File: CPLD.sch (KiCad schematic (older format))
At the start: 35 parts, among them J5 JTAG, SW2 SW_DIP_x06, SW3 User PB, U12 74HCT3G04, U3 EPM7064STC100, X1 CFPS-72 50mhz

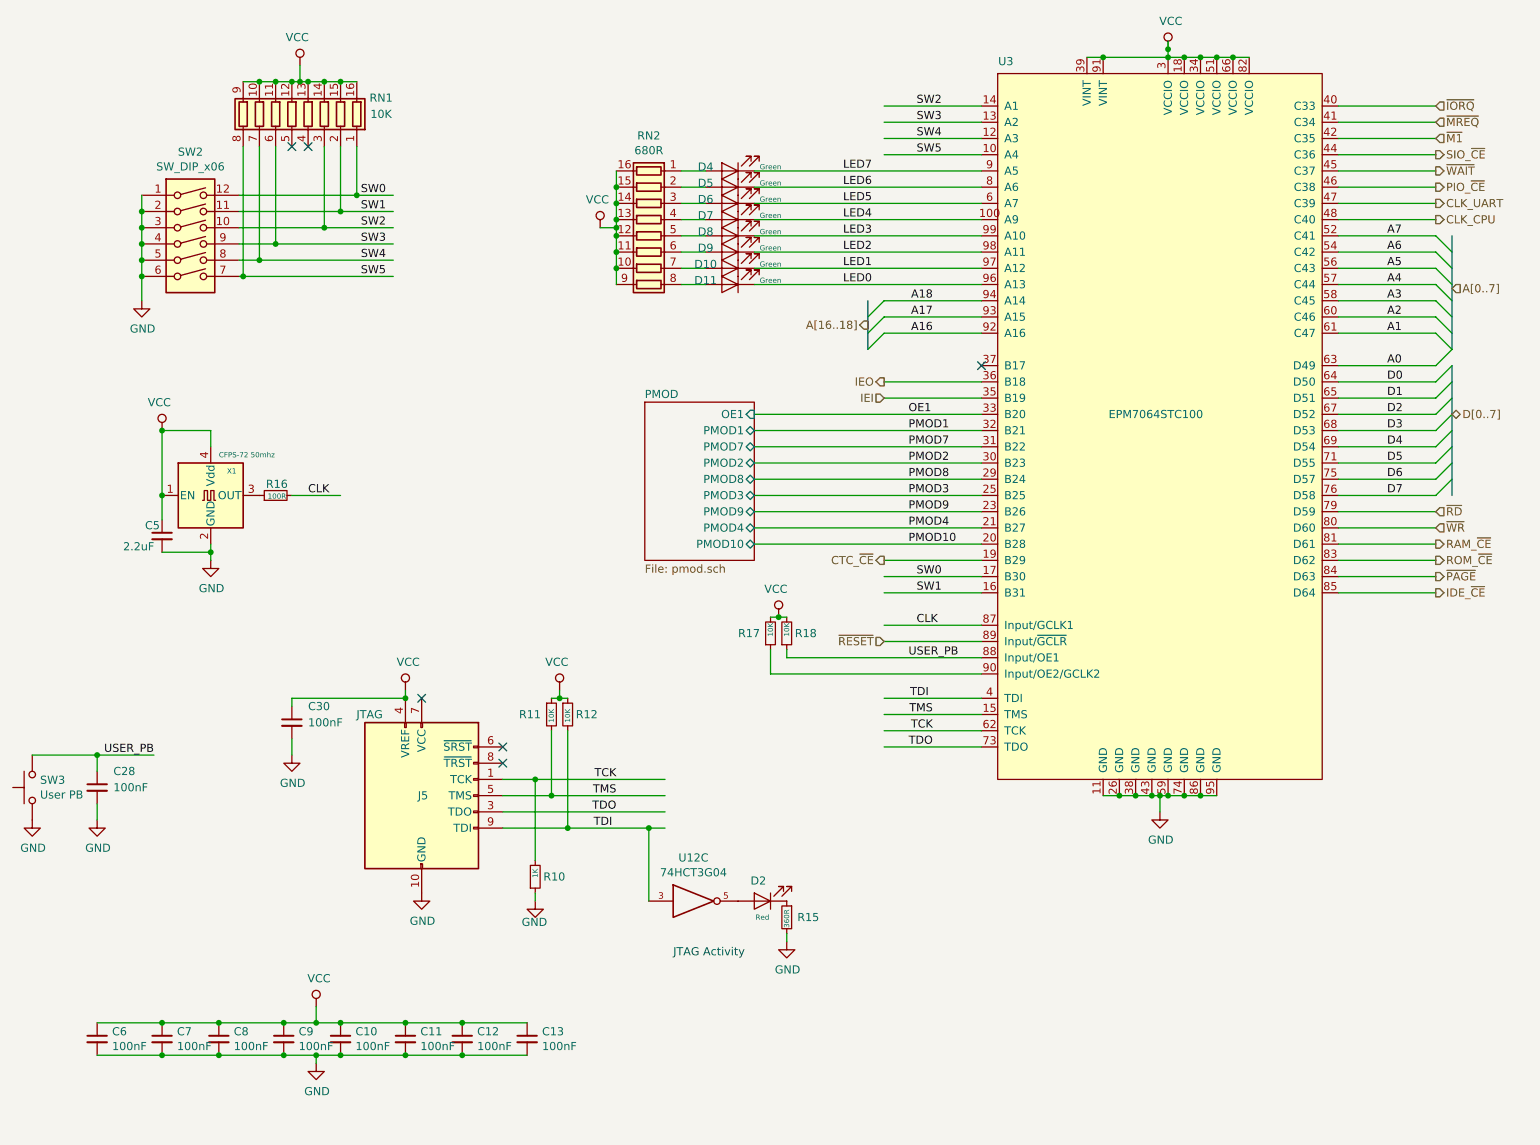
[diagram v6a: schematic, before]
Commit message: replaced VCC with 5V, fixed ROM footprint
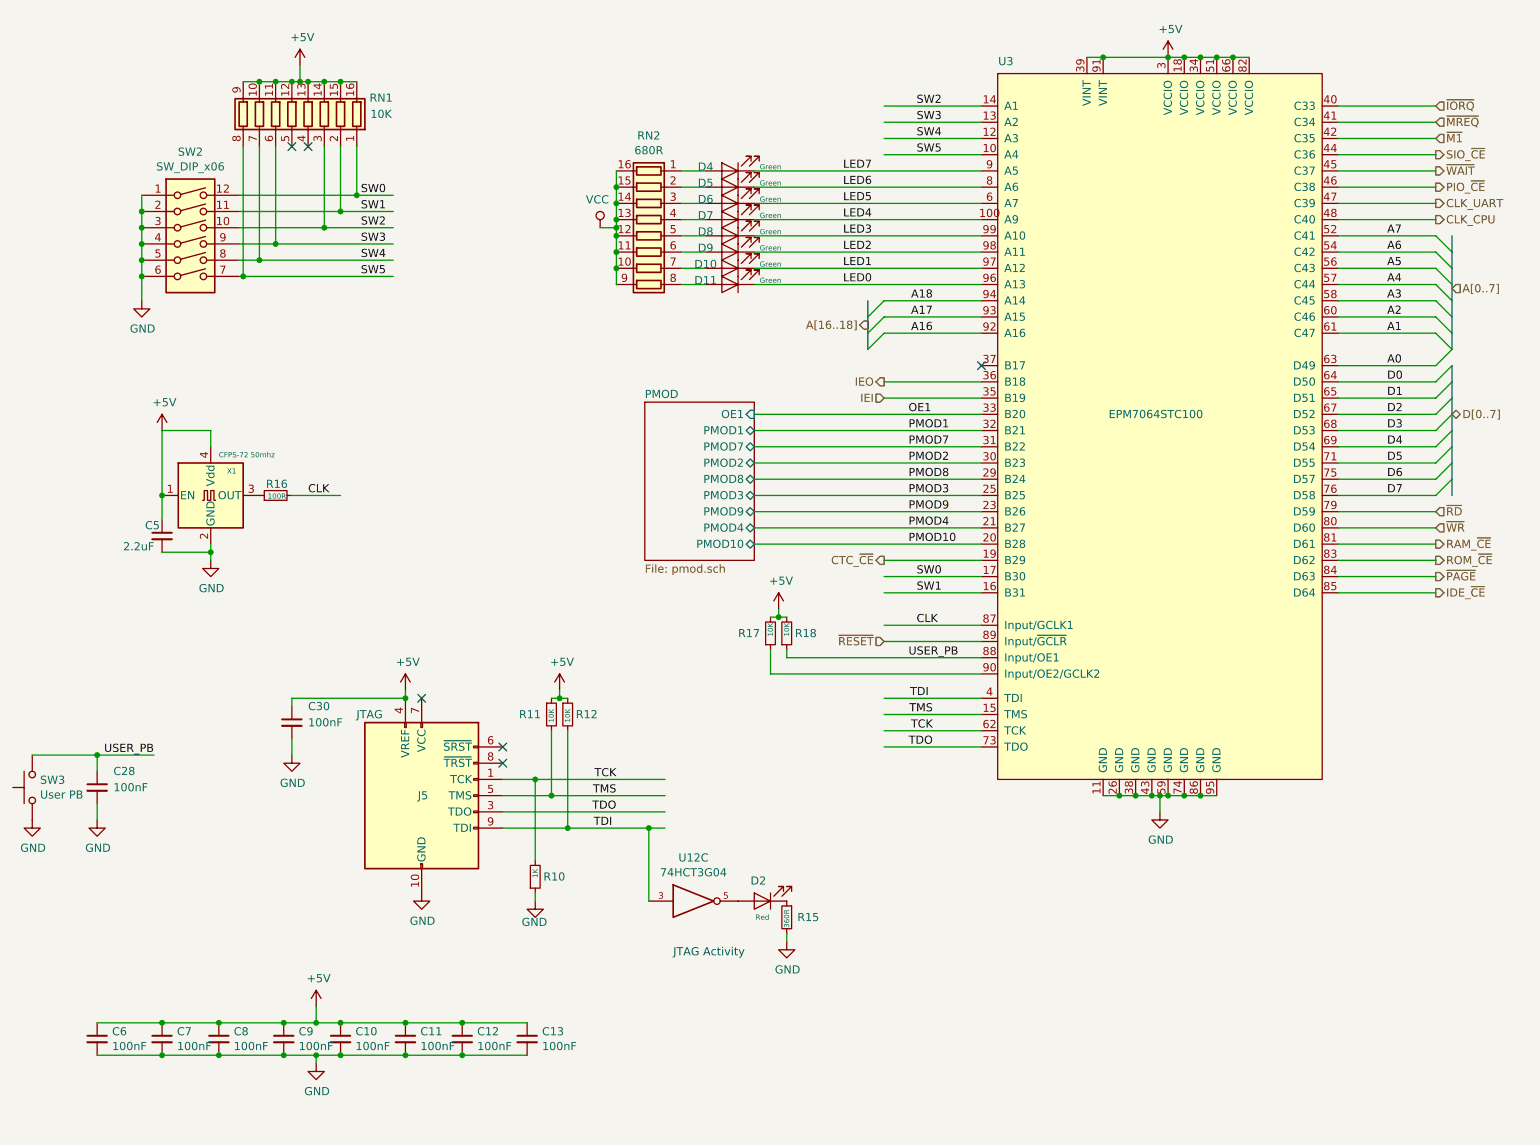
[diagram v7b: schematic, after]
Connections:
- net labels added: +5V
- wire segments 190 -> 189
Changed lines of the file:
@@
 	1    0    0    -1
-$EndComp
-Connection ~ 1700 3250
-$Comp
-L power:VCC #PWR?
-U 1 1 5DB43EF8
-P 1700 3250
-AR Path="/5DB43EF8" Ref="#PWR?"  Part="1"
-AR Path="/5D70CA34/5DB43EF8" Ref="#PWR023"  Part="1"
-F 0 "#PWR023" H 1700 3100 50  0001 C CNN
-F 1 "VCC" H 1717 3423 50  0000 C CNN
-F 2 "" H 1700 3250 50  0001 C CNN
-F 3 "" H 1700 3250 50  0001 C CNN
-	1    1700 3250
-	-1   0    0    -1
 $EndComp
 $Comp
@@
 	-1   0    0    -1
 $EndComp
-$Comp
-L power:VCC #PWR?
-U 1 1 5DC12FAB
-P 3200 4850
-AR Path="/5DC12FAB" Ref="#PWR?"  Part="1"
-AR Path="/5D70CA34/5DC12FAB" Ref="#PWR020"  Part="1"
-F 0 "#PWR020" H 3200 4700 50  0001 C CNN
-F 1 "VCC" H 3217 5023 50  0000 C CNN
-F 2 "" H 3200 4850 50  0001 C CNN
-F 3 "" H 3200 4850 50  0001 C CNN
-	1    3200 4850
-	1    0    0    -1
-$EndComp
 Wire Wire Line
 	3800 5400 4000 5400
@@
 $EndComp
 Connection ~ 7900 950
-$Comp
-L power:VCC #PWR?
-U 1 1 5DF027A6
-P 7900 900
-AR Path="/5DF027A6" Ref="#PWR?"  Part="1"
-AR Path="/5D70CA34/5DF027A6" Ref="#PWR032"  Part="1"
-F 0 "#PWR032" H 7900 750 50  0001 C CNN
-F 1 "VCC" H 7917 1073 50  0000 C CNN
-F 2 "" H 7900 900 50  0001 C CNN
-F 3 "" H 7900 900 50  0001 C CNN
-	1    7900 900
-	1    0    0    -1
-$EndComp
-Wire Wire Line
-	7900 950  7900 900
 Wire Wire Line
 	7850 5500 7850 5600
@@
 Wire Wire Line
 	3550 7100 3200 7100
-$Comp
-L power:VCC #PWR?
-U 1 1 5FB8A6EC
-P 2650 6800
-AR Path="/5FB8A6EC" Ref="#PWR?"  Part="1"
-AR Path="/5D70CA34/5FB8A6EC" Ref="#PWR029"  Part="1"
-F 0 "#PWR029" H 2650 6650 50  0001 C CNN
-F 1 "VCC" H 2667 6973 50  0000 C CNN
-F 2 "" H 2650 6800 50  0001 C CNN
-F 3 "" H 2650 6800 50  0001 C CNN
-	1    2650 6800
-	1    0    0    -1
-$EndComp
 Wire Wire Line
 	2650 6900 2650 6800
@@
 OE1
 NoConn ~ 6750 2850
-Connection ~ 7900 900
-Wire Wire Line
-	7900 900  7900 850
 Wire Wire Line
 	5350 1750 6750 1750
@@
 Wire Wire Line
 	5350 1650 6750 1650
-$Comp
-L power:VCC #PWR?
-U 1 1 5D9F3379
-P 5500 4400
-AR Path="/5D9F3379" Ref="#PWR?"  Part="1"
-AR Path="/5D70CA34/5D9F3379" Ref="#PWR0102"  Part="1"
-F 0 "#PWR0102" H 5500 4250 50  0001 C CNN
-F 1 "VCC" H 5517 4573 50  0000 C CNN
-F 2 "" H 5500 4400 50  0001 C CNN
-F 3 "" H 5500 4400 50  0001 C CNN
-	1    5500 4400
-	-1   0    0    -1
-$EndComp
 Text Label 2600 3650 0    50   ~ 0
 CLK
@@
 Wire Wire Line
 	2550 1100 2500 1100
-$Comp
-L power:VCC #PWR024
-U 1 1 5D7E678A
-P 2550 1000
-F 0 "#PWR024" H 2550 850 50  0001 C CNN
-F 1 "VCC" H 2567 1173 50  0000 C CNN
-F 2 "" H 2550 1000 50  0001 C CNN
-F 3 "" H 2550 1000 50  0001 C CNN
-	1    2550 1000
-	-1   0    0    -1
-$EndComp
 Wire Wire Line
 	2700 1500 2700 2000
@@
 IEO
 Wire Wire Line
-	5450 4400 5500 4400
-Connection ~ 5500 4400
-Wire Wire Line
-	5500 4400 5550 4400
-Wire Wire Line
 	5550 4600 5550 4650
 Wire Wire Line
@@
 Wire Wire Line
 	3800 5700 4200 5700
-$Comp
-L power:VCC #PWR?
-U 1 1 5DA39994
-P 4150 4850
-AR Path="/5DA39994" Ref="#PWR?"  Part="1"
-AR Path="/5D70CA34/5DA39994" Ref="#PWR022"  Part="1"
-F 0 "#PWR022" H 4150 4700 50  0001 C CNN
-F 1 "VCC" H 4167 5023 50  0000 C CNN
-F 2 "" H 4150 4850 50  0001 C CNN
-F 3 "" H 4150 4850 50  0001 C CNN
-	1    4150 4850
-	-1   0    0    -1
-$EndComp
 Wire Wire Line
 	4150 4850 4150 4900
@@
 	2500 4900 3200 4900
 Connection ~ 3200 4900
+$Comp
+L power:+5V #PWR?
+U 1 1 5EB28D79
+P 7900 950
+AR Path="/5D70CA34/5DC790D1/5EB28D79" Ref="#PWR?"  Part="1"
+AR Path="/5D70CA34/5EB28D79" Ref="#PWR0121"  Part="1"
+F 0 "#PWR0121" H 7900 800 50  0001 C CNN
+F 1 "+5V" H 7915 1123 50  0000 C CNN
+F 2 "" H 7900 950 50  0001 C CNN
+F 3 "" H 7900 950 50  0001 C CNN
+	1    7900 950
+	1    0    0    -1
+$EndComp
+$Comp
+L power:+5V #PWR?
+U 1 1 5EB440A1
+P 2550 1000
+AR Path="/5D70CA34/5DC790D1/5EB440A1" Ref="#PWR?"  Part="1"
+AR Path="/5D70CA34/5EB440A1" Ref="#PWR0122"  Part="1"
+F 0 "#PWR0122" H 2550 850 50  0001 C CNN
+F 1 "+5V" H 2565 1173 50  0000 C CNN
+F 2 "" H 2550 1000 50  0001 C CNN
+F 3 "" H 2550 1000 50  0001 C CNN
+	1    2550 1000
+	1    0    0    -1
+$EndComp
+$Comp
+L power:+5V #PWR?
+U 1 1 5EB7B4D6
+P 1700 3250
+AR Path="/5D70CA34/5DC790D1/5EB7B4D6" Ref="#PWR?"  Part="1"
+AR Path="/5D70CA34/5EB7B4D6" Ref="#PWR0123"  Part="1"
+F 0 "#PWR0123" H 1700 3100 50  0001 C CNN
+F 1 "+5V" H 1715 3423 50  0000 C CNN
+F 2 "" H 1700 3250 50  0001 C CNN
+F 3 "" H 1700 3250 50  0001 C CNN
+	1    1700 3250
+	1    0    0    -1
+$EndComp
+$Comp
+L power:+5V #PWR?
+U 1 1 5EB9676C
+P 3200 4850
+AR Path="/5D70CA34/5DC790D1/5EB9676C" Ref="#PWR?"  Part="1"
+AR Path="/5D70CA34/5EB9676C" Ref="#PWR0124"  Part="1"
+F 0 "#PWR0124" H 3200 4700 50  0001 C CNN
+F 1 "+5V" H 3215 5023 50  0000 C CNN
+F 2 "" H 3200 4850 50  0001 C CNN
+F 3 "" H 3200 4850 50  0001 C CNN
+	1    3200 4850
+	1    0    0    -1
+$EndComp
+$Comp
+L power:+5V #PWR?
+U 1 1 5EBB1BE7
+P 4150 4850
+AR Path="/5D70CA34/5DC790D1/5EBB1BE7" Ref="#PWR?"  Part="1"
+AR Path="/5D70CA34/5EBB1BE7" Ref="#PWR0125"  Part="1"
+F 0 "#PWR0125" H 4150 4700 50  0001 C CNN
+F 1 "+5V" H 4165 5023 50  0000 C CNN
+F 2 "" H 4150 4850 50  0001 C CNN
+F 3 "" H 4150 4850 50  0001 C CNN
+	1    4150 4850
+	1    0    0    -1
+$EndComp
+$Comp
+L power:+5V #PWR?
+U 1 1 5EBCCE40
+P 2650 6800
+AR Path="/5D70CA34/5DC790D1/5EBCCE40" Ref="#PWR?"  Part="1"
+AR Path="/5D70CA34/5EBCCE40" Ref="#PWR0126"  Part="1"
+F 0 "#PWR0126" H 2650 6650 50  0001 C CNN
+F 1 "+5V" H 2665 6973 50  0000 C CNN
+F 2 "" H 2650 6800 50  0001 C CNN
+F 3 "" H 2650 6800 50  0001 C CNN
+	1    2650 6800
+	1    0    0    -1
+$EndComp
+Wire Wire Line
+	5450 4400 5500 4400
+$Comp
+L power:+5V #PWR?
+U 1 1 5F1064BC
+P 5500 4350
+AR Path="/5D70CA34/5DC790D1/5F1064BC" Ref="#PWR?"  Part="1"
+AR Path="/5D70CA34/5F1064BC" Ref="#PWR0127"  Part="1"
+F 0 "#PWR0127" H 5500 4200 50  0001 C CNN
+F 1 "+5V" H 5515 4523 50  0000 C CNN
+F 2 "" H 5500 4350 50  0001 C CNN
+F 3 "" H 5500 4350 50  0001 C CNN
+	1    5500 4350
+	1    0    0    -1
+$EndComp
+Wire Wire Line
+	5500 4350 5500 4400
 Wire Bus Line
 	6050 2450 6050 2750
@@
 Wire Bus Line
 	9650 2850 9650 3650
+Connection ~ 5500 4400
+Wire Wire Line
+	5500 4400 5550 4400
 $EndSCHEMATC

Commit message: layout changes, silkscreen fixes
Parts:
- U8: renamed from U12; value 74HCT3G04 -> 74LVC1G04; footprint Package_SO:TSSOP-8_3x3mm_P0.65mm -> Package_SO:TSOP-5_1.65x3.05mm_P0.95mm; symbol THS-80-rescue:74HCT3G04-74xGxx -> 74xGxx:74LVC1G04
- renumbered C5 to C11, C30 to C12, C28 to C13, C6 to C14, C7 to C15, C8 to C16, C9 to C17, C10 to C18, C11 to C19, C12 to C20, C13 to C21, D9 to D10, D10 to D11, D11 to D12, D2 to D13, D4 to D5, D5 to D6, D6 to D7, D7 to D8, D8 to D9, J5 to J4, R16 to R13, R17 to R14, R18 to R15, R11 to R16, R12 to R17, R10 to R18, R15 to R19, U3 to U7
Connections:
- net labels removed: +5V
- wire segments 189 -> 186
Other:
- moved on the sheet: R15
